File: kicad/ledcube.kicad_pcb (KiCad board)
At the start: 2 copper layers, 45 x 45 mm, 49 parts, among them P1 USB_C_Plug_USB2.0, SW1 SW_SPDT_321, SW2 SW_SPDT_321, SW3 SW_SPDT_321

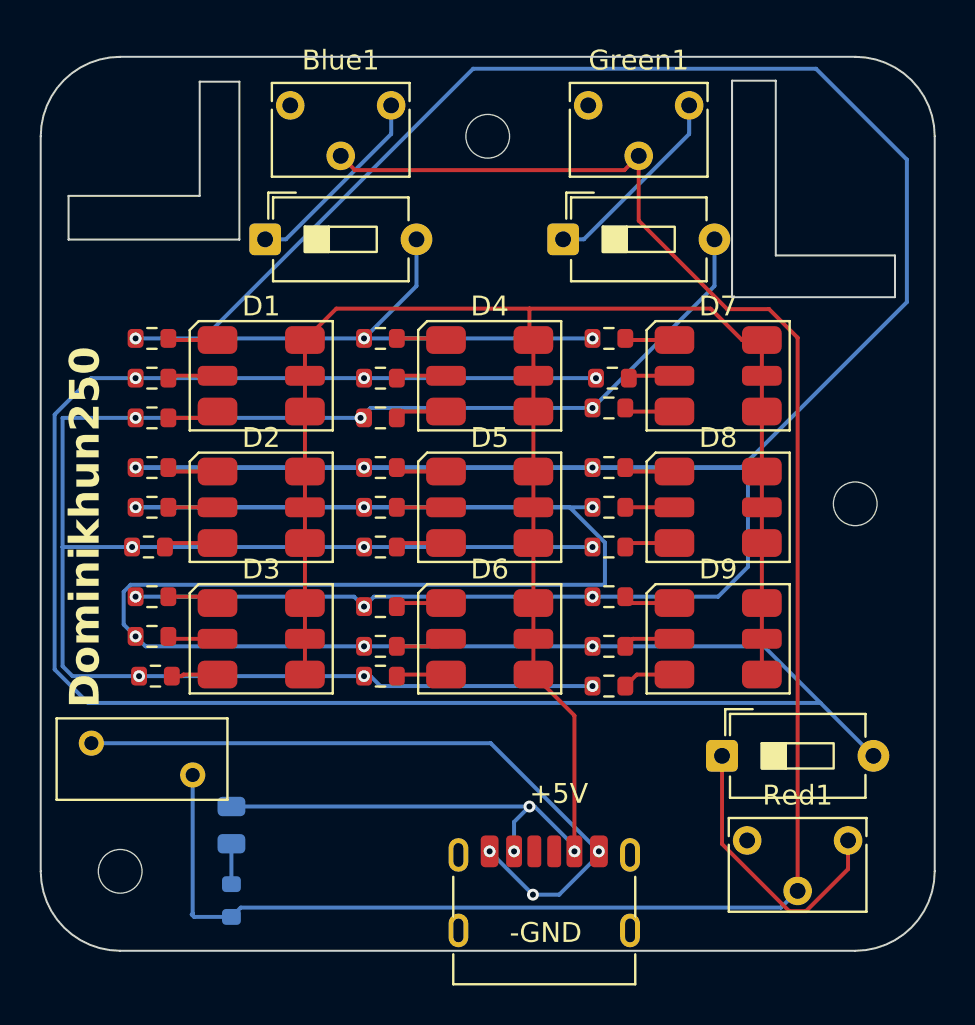
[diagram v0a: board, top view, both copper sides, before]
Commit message: Added 12V support for Motherboards
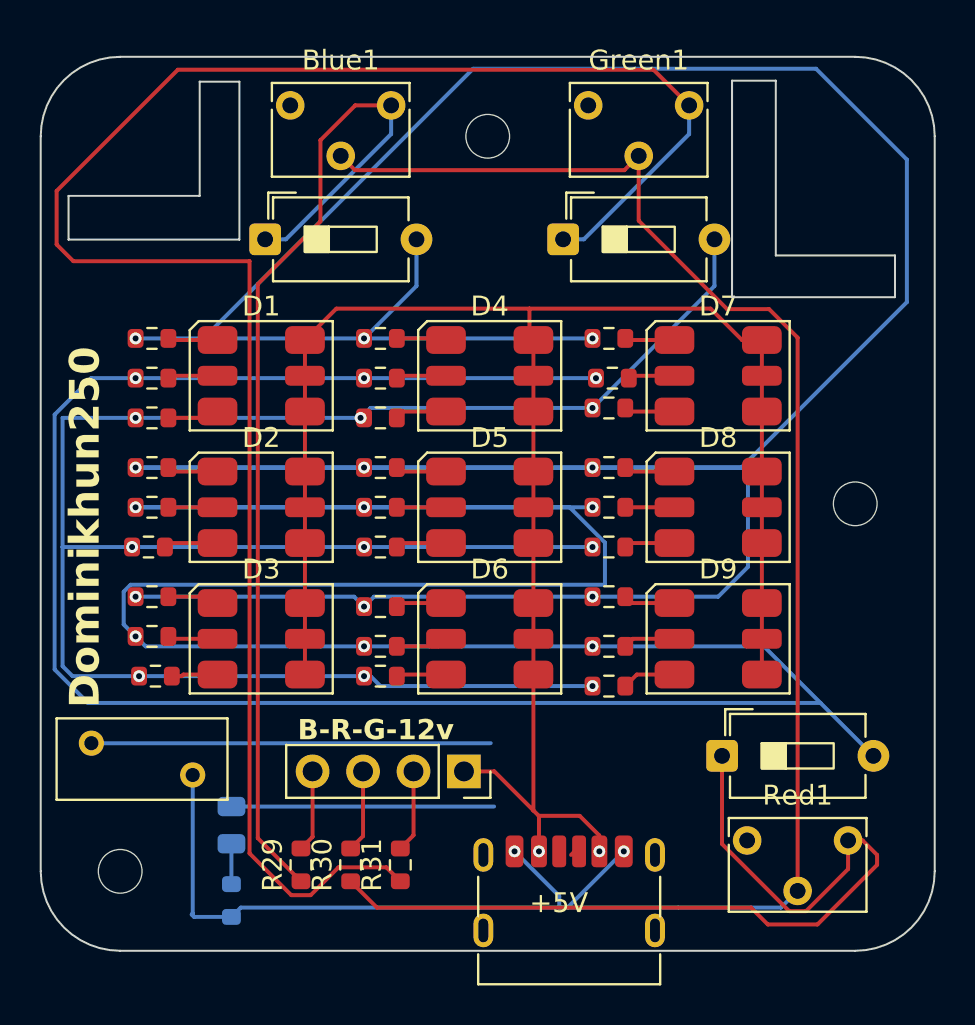
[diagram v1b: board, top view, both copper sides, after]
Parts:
- added J1: Conn_01x04, Connector_PinSocket_2.54mm:PinSocket_1x04_P2.54mm_Vertical, F.Cu at (101.2, 92.3)
- added R29: 400R, Resistor_SMD:R_0603_1608Metric, F.Cu at (93.0, 97.0)
- added R30: 400R, Resistor_SMD:R_0603_1608Metric, F.Cu at (95.5, 97.0)
- added R31: 400R, Resistor_SMD:R_0603_1608Metric, F.Cu at (98.0, 97.0)
- moved P1 1.25 mm to (106.5, 99.5)
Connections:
- Blue1 pad 1: Net-(SW3-C) -> Net-(Blue1-Pad1)
- Green1 pad 1: Net-(SW1-C) -> Net-(Green1-Pad1)
- P1 pad A12: Net-(F1-Pad1) -> Net-(Blue1-Pad2)
- P1 pad B12: Net-(F1-Pad1) -> Net-(Blue1-Pad2)
- R1 pad 2: Net-(SW1-B) -> Net-(Green1-Pad1)
- R10 pad 2: Net-(SW1-B) -> Net-(Green1-Pad1)
- R11 pad 2: Net-(SW2-B) -> Net-(R11-Pad2)
- R12 pad 2: Net-(SW3-B) -> Net-(Blue1-Pad1)
- R13 pad 2: Net-(SW1-B) -> Net-(Green1-Pad1)
- R14 pad 2: Net-(SW2-B) -> Net-(R11-Pad2)
- R15 pad 2: Net-(SW3-B) -> Net-(Blue1-Pad1)
- R16 pad 2: Net-(SW1-B) -> Net-(Green1-Pad1)
- R17 pad 2: Net-(SW2-B) -> Net-(R11-Pad2)
- R18 pad 2: Net-(SW3-B) -> Net-(Blue1-Pad1)
- R19 pad 2: Net-(SW1-B) -> Net-(Green1-Pad1)
- R2 pad 2: Net-(SW2-B) -> Net-(R11-Pad2)
- R20 pad 2: Net-(SW2-B) -> Net-(R11-Pad2)
- R21 pad 2: Net-(SW3-B) -> Net-(Blue1-Pad1)
- R22 pad 2: Net-(SW1-B) -> Net-(Green1-Pad1)
- R23 pad 2: Net-(SW2-B) -> Net-(R11-Pad2)
- R24 pad 2: Net-(SW3-B) -> Net-(Blue1-Pad1)
- R25 pad 2: Net-(SW1-B) -> Net-(Green1-Pad1)
- R26 pad 2: Net-(SW2-B) -> Net-(R11-Pad2)
- R27 pad 2: Net-(SW3-B) -> Net-(Blue1-Pad1)
- R3 pad 2: Net-(SW3-B) -> Net-(Blue1-Pad1)
- R4 pad 2: Net-(SW1-B) -> Net-(Green1-Pad1)
- R5 pad 2: Net-(SW2-B) -> Net-(R11-Pad2)
- R6 pad 2: Net-(SW3-B) -> Net-(Blue1-Pad1)
- R7 pad 2: Net-(SW1-B) -> Net-(Green1-Pad1)
- R8 pad 2: Net-(SW2-B) -> Net-(R11-Pad2)
- R9 pad 2: Net-(SW3-B) -> Net-(Blue1-Pad1)
- Red1 pad 1: Net-(SW2-C) -> Net-(R11-Pad2)
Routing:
- net Net-(Green1-Pad1): track 0.00 -> 87.0 mm
- net Net-(Blue1-Pad1): track 0.00 -> 43.8 mm
- net Net-(R11-Pad2): track 0.00 -> 30.5 mm
- net Net-(F1-Pad1): track 35.0 -> 20.1 mm, vias 3 -> 0
- net Net-(Blue1-Pad2): track 95.3 -> 103.6 mm, vias 0 -> 2
- net Net-(J1-Pin_2): track 0.00 -> 4.16 mm
- net Net-(J1-Pin_3): track 0.00 -> 4.14 mm
- net Net-(J1-Pin_4): track 0.00 -> 4.12 mm
- net unconnected-(P1-VCONN-PadB5): track 0.00 -> 0.78 mm
- net Net-(D1-AB): track 108.0 -> 107.3 mm, vias 3 -> 2
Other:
- board text added: "B-R-G-12v"
- board text removed: "-GND"

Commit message: Revert "Added 12V support for Motherboards"
This reverts commit cbf7dcde6a27399269292319d1f5b2d3f34ebe3c.
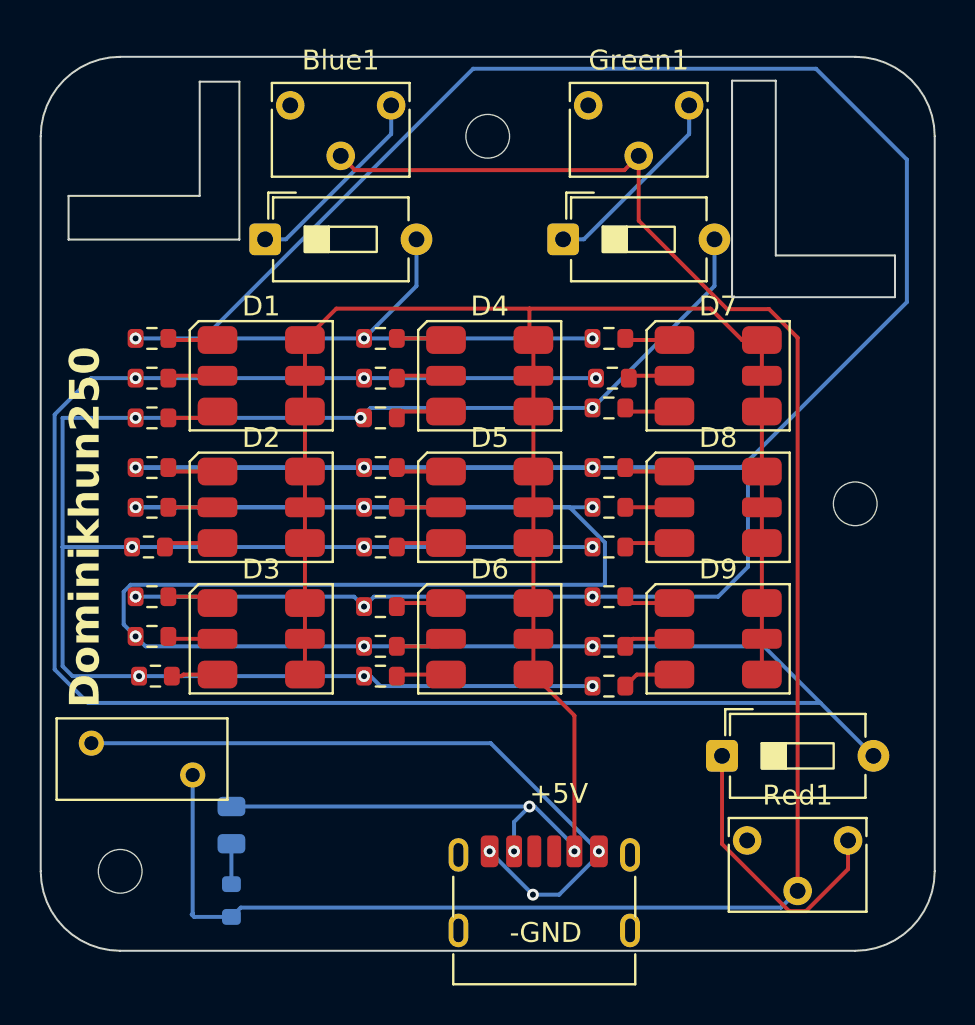
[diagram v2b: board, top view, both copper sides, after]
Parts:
- removed J1: Conn_01x04, Connector_PinSocket_2.54mm:PinSocket_1x04_P2.54mm_Vertical
- removed R29, R30, R31: 400R, Resistor_SMD:R_0603_1608Metric
- moved P1 1.25 mm to (105.2, 99.5)
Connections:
- Blue1 pad 1: Net-(Blue1-Pad1) -> Net-(SW3-C)
- Green1 pad 1: Net-(Green1-Pad1) -> Net-(SW1-C)
- P1 pad A12: Net-(Blue1-Pad2) -> Net-(F1-Pad1)
- P1 pad B12: Net-(Blue1-Pad2) -> Net-(F1-Pad1)
- R1 pad 2: Net-(Green1-Pad1) -> Net-(SW1-B)
- R10 pad 2: Net-(Green1-Pad1) -> Net-(SW1-B)
- R11 pad 2: Net-(R11-Pad2) -> Net-(SW2-B)
- R12 pad 2: Net-(Blue1-Pad1) -> Net-(SW3-B)
- R13 pad 2: Net-(Green1-Pad1) -> Net-(SW1-B)
- R14 pad 2: Net-(R11-Pad2) -> Net-(SW2-B)
- R15 pad 2: Net-(Blue1-Pad1) -> Net-(SW3-B)
- R16 pad 2: Net-(Green1-Pad1) -> Net-(SW1-B)
- R17 pad 2: Net-(R11-Pad2) -> Net-(SW2-B)
- R18 pad 2: Net-(Blue1-Pad1) -> Net-(SW3-B)
- R19 pad 2: Net-(Green1-Pad1) -> Net-(SW1-B)
- R2 pad 2: Net-(R11-Pad2) -> Net-(SW2-B)
- R20 pad 2: Net-(R11-Pad2) -> Net-(SW2-B)
- R21 pad 2: Net-(Blue1-Pad1) -> Net-(SW3-B)
- R22 pad 2: Net-(Green1-Pad1) -> Net-(SW1-B)
- R23 pad 2: Net-(R11-Pad2) -> Net-(SW2-B)
- R24 pad 2: Net-(Blue1-Pad1) -> Net-(SW3-B)
- R25 pad 2: Net-(Green1-Pad1) -> Net-(SW1-B)
- R26 pad 2: Net-(R11-Pad2) -> Net-(SW2-B)
- R27 pad 2: Net-(Blue1-Pad1) -> Net-(SW3-B)
- R3 pad 2: Net-(Blue1-Pad1) -> Net-(SW3-B)
- R4 pad 2: Net-(Green1-Pad1) -> Net-(SW1-B)
- R5 pad 2: Net-(R11-Pad2) -> Net-(SW2-B)
- R6 pad 2: Net-(Blue1-Pad1) -> Net-(SW3-B)
- R7 pad 2: Net-(Green1-Pad1) -> Net-(SW1-B)
- R8 pad 2: Net-(R11-Pad2) -> Net-(SW2-B)
- R9 pad 2: Net-(Blue1-Pad1) -> Net-(SW3-B)
- Red1 pad 1: Net-(R11-Pad2) -> Net-(SW2-C)
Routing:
- net Net-(Green1-Pad1): track 87.0 -> 0.00 mm
- net Net-(Blue1-Pad1): track 43.8 -> 0.00 mm
- net Net-(R11-Pad2): track 30.5 -> 0.00 mm
- net Net-(F1-Pad1): track 20.1 -> 35.0 mm, vias 0 -> 3
- net Net-(Blue1-Pad2): track 103.6 -> 95.3 mm, vias 2 -> 0
- net Net-(J1-Pin_2): track 4.16 -> 0.00 mm
- net Net-(J1-Pin_3): track 4.14 -> 0.00 mm
- net Net-(J1-Pin_4): track 4.12 -> 0.00 mm
- net unconnected-(P1-VCONN-PadB5): track 0.78 -> 0.00 mm
- net Net-(D1-AB): track 107.3 -> 108.0 mm, vias 2 -> 3
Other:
- board text added: "-GND"
- board text removed: "B-R-G-12v"
